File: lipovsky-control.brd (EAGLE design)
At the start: 59 x 32 mm, 44 parts, among them J5 AVRISP0.1", P1 M04-929P, P2 M04-929P, P3 M04-929P, P4 M04-929P, U1 ATTINYX4A8MU, U2 MIC2288YD5, U3 MIC2288YD5, U4 LTV-816S

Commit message: tidy
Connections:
- removed net !OE: J5.3, P3.3, U1.1
- removed net CP: J5.1, P3.2, U1.20
- removed net DS: J5.4, P3.1, U1.16
- new net !S_RESET: P3.1
- new net MISO: J5.1, U1.20
- new net SCL: J5.3, P3.2, U1.1
- new net SDA: J5.4, P3.3, U1.16
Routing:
- net !OE: track 40.7 -> 0.00 mm
- net CP: track 39.9 -> 0.00 mm
- net SDA: track 0.00 -> 38.6 mm, vias 0 -> 1
- net SCL: track 0.00 -> 38.1 mm
- net DS: track 31.9 -> 0.00 mm, vias 1 -> 0
- net MISO: track 0.00 -> 6.01 mm
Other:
- board text added: "SCL"
- board text added: "SDA"
- board text removed: "!OE"
- board text removed: "CP"
- board text removed: "DS"
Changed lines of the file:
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@@
 <wire x1="1.5" y1="8.75" x2="1.5" y2="8.25" width="0.15" layer="21"/>
 <text x="51.9" y="28.4" size="0.8" layer="21" font="vector" ratio="15" align="top-center">S-</text>
-<text x="49.3" y="28.4" size="0.8" layer="21" font="vector" ratio="15" align="top-center">!OE</text>
-<text x="46.8" y="28.4" size="0.8" layer="21" font="vector" ratio="15" align="top-center">CP</text>
-<text x="44.3" y="28.4" size="0.8" layer="21" font="vector" ratio="15" align="top-center">DS</text>
+<text x="49.3" y="28.4" size="0.8" layer="21" font="vector" ratio="15" align="top-center">SDA</text>
+<text x="46.8" y="28.4" size="0.8" layer="21" font="vector" ratio="15" align="top-center">SCL</text>
 <text x="16.2" y="28.7" size="0.8" layer="21" font="vector" ratio="15" align="top-center">+8V</text>
 <text x="18.8" y="28.7" size="0.8" layer="21" font="vector" ratio="15" align="top-center">+5V</text>
@@
 <wire x1="35.4" y1="10.84" x2="34.54" y2="11.7" width="0.3" layer="1"/>
 <wire x1="36.5" y1="2.7" x2="35.4" y2="3.8" width="0.3" layer="1"/>
-<wire x1="51.81" y1="30" x2="50.51" y2="28.7" width="0.3" layer="1"/>
-<wire x1="50.51" y1="28.7" x2="42.4" y2="28.7" width="0.3" layer="1"/>
-<wire x1="42.4" y1="28.7" x2="36.6" y2="22.9" width="0.3" layer="1"/>
-<wire x1="36.6" y1="22.9" x2="30.2" y2="22.9" width="0.3" layer="1"/>
-<wire x1="30.2" y1="22.9" x2="29.4" y2="22.1" width="0.3" layer="1"/>
-<wire x1="29.4" y1="22.1" x2="25.7" y2="22.1" width="0.3" layer="1"/>
+<wire x1="51.81" y1="30" x2="50.41" y2="28.6" width="0.3" layer="1"/>
+<wire x1="50.41" y1="28.6" x2="42.3" y2="28.6" width="0.3" layer="1"/>
+<wire x1="42.3" y1="28.6" x2="36.6" y2="22.9" width="0.3" layer="1"/>
+<wire x1="36.6" y1="22.9" x2="30.7" y2="22.9" width="0.3" layer="1"/>
+<wire x1="30.7" y1="22.9" x2="29.9" y2="22.1" width="0.3" layer="1"/>
+<wire x1="29.9" y1="22.1" x2="25.7" y2="22.1" width="0.3" layer="1"/>
 <wire x1="25.7" y1="22.1" x2="25.45" y2="22.35" width="0.3" layer="1"/>
 <wire x1="25.45" y1="22.35" x2="25.45" y2="22.55" width="0.3" layer="1"/>
@@
 <via x="20" y="28.9" extent="1-16" drill="0.35"/>
 </signal>
-<signal name="!OE">
-<contactref element="U1" pad="1"/>
-<contactref element="J5" pad="3"/>
-<contactref element="P3" pad="3"/>
-<wire x1="21.9" y1="22" x2="22.075" y2="22" width="0.25" layer="1"/>
-<wire x1="22.075" y1="22" x2="22.075" y2="20.025" width="0.25" layer="1"/>
-<wire x1="22.075" y1="20.025" x2="23.275" y2="18.825" width="0.25" layer="1"/>
-<wire x1="23.275" y1="18.825" x2="23.275" y2="17.005" width="0.25" layer="1"/>
-<wire x1="23.275" y1="17.005" x2="22" y2="15.73" width="0.25" layer="1"/>
-<wire x1="47.37" y1="28.1" x2="42.7" y2="28.1" width="0.3" layer="16"/>
-<wire x1="42.7" y1="28.1" x2="36.9" y2="22.3" width="0.3" layer="16"/>
-<wire x1="36.9" y1="22.3" x2="30.4" y2="22.3" width="0.3" layer="16"/>
-<wire x1="30.4" y1="22.3" x2="25.1" y2="17" width="0.3" layer="16"/>
-<wire x1="25.1" y1="17" x2="23.43" y2="17" width="0.3" layer="16"/>
-<wire x1="23.43" y1="17" x2="22.16" y2="15.73" width="0.3" layer="16"/>
-<wire x1="22.16" y1="15.73" x2="22" y2="15.73" width="0.3" layer="16"/>
-<wire x1="47.37" y1="28.1" x2="49.27" y2="30" width="0.3" layer="16"/>
-</signal>
-<signal name="CP">
+<signal name="MISO">
 <contactref element="U1" pad="20"/>
 <contactref element="J5" pad="1"/>
-<contactref element="P3" pad="2"/>
 <wire x1="21" y1="21.1" x2="21" y2="19.2" width="0.25" layer="1"/>
 <wire x1="21" y1="19.2" x2="20.725" y2="18.925" width="0.25" layer="1"/>
 <wire x1="20.725" y1="18.925" x2="20.725" y2="16.995" width="0.25" layer="1"/>
 <wire x1="20.725" y1="16.995" x2="19.46" y2="15.73" width="0.25" layer="1"/>
-<wire x1="45.43" y1="28.7" x2="42.4" y2="28.7" width="0.3" layer="16"/>
-<wire x1="42.4" y1="28.7" x2="36.6" y2="22.9" width="0.3" layer="16"/>
-<wire x1="36.6" y1="22.9" x2="30.2" y2="22.9" width="0.3" layer="16"/>
-<wire x1="30.2" y1="22.9" x2="26.9" y2="19.6" width="0.3" layer="16"/>
-<wire x1="26.9" y1="19.6" x2="24" y2="19.6" width="0.3" layer="16"/>
-<wire x1="24" y1="19.6" x2="23.275" y2="18.875" width="0.3" layer="16"/>
-<wire x1="23.275" y1="18.875" x2="23.275" y2="17.675" width="0.3" layer="16"/>
-<wire x1="23.275" y1="17.675" x2="22.6" y2="17" width="0.3" layer="16"/>
-<wire x1="22.6" y1="17" x2="20.73" y2="17" width="0.3" layer="16"/>
-<wire x1="20.73" y1="17" x2="19.46" y2="15.73" width="0.3" layer="16"/>
-<wire x1="45.43" y1="28.7" x2="46.73" y2="30" width="0.3" layer="16"/>
-</signal>
-<signal name="DS">
-<contactref element="U1" pad="16"/>
-<contactref element="J5" pad="4"/>
-<contactref element="P3" pad="1"/>
-<via x="20.2" y="19.6" extent="1-16" drill="0.35"/>
-<wire x1="19" y1="21.1" x2="19" y2="20.6" width="0.25" layer="1"/>
-<wire x1="19" y1="20.6" x2="19.2" y2="20.4" width="0.25" layer="1"/>
-<wire x1="19.2" y1="20.4" x2="19.9" y2="20.4" width="0.25" layer="1"/>
-<wire x1="19.9" y1="20.4" x2="20.2" y2="20.1" width="0.25" layer="1"/>
-<wire x1="20.2" y1="20.1" x2="20.2" y2="19.6" width="0.25" layer="1"/>
-<wire x1="20.67" y1="19.6" x2="22" y2="18.27" width="0.3" layer="16"/>
-<wire x1="26.7" y1="20.2" x2="30" y2="23.5" width="0.3" layer="16"/>
-<wire x1="30" y1="23.5" x2="36.3" y2="23.5" width="0.3" layer="16"/>
-<wire x1="36.3" y1="23.5" x2="42.1" y2="29.3" width="0.3" layer="16"/>
-<wire x1="26.7" y1="20.2" x2="23.83" y2="20.2" width="0.3" layer="16"/>
-<wire x1="20.67" y1="19.6" x2="20.2" y2="19.6" width="0.3" layer="16"/>
-<wire x1="23.83" y1="20.2" x2="22" y2="18.37" width="0.3" layer="16"/>
-<wire x1="22" y1="18.37" x2="22" y2="18.27" width="0.3" layer="16"/>
-<wire x1="42.1" y1="29.3" x2="43.49" y2="29.3" width="0.3" layer="16"/>
-<wire x1="43.49" y1="29.3" x2="44.19" y2="30" width="0.3" layer="16"/>
 </signal>
 <signal name="S+">
@@
 <contactref element="P1" pad="1"/>
 </signal>
+<signal name="SDA">
+<contactref element="P3" pad="3"/>
+<contactref element="U1" pad="16"/>
+<contactref element="J5" pad="4"/>
+<via x="20.2" y="19.6" extent="1-16" drill="0.35"/>
+<wire x1="19" y1="21.1" x2="19" y2="20.6" width="0.25" layer="1"/>
+<wire x1="19" y1="20.6" x2="19.2" y2="20.4" width="0.25" layer="1"/>
+<wire x1="19.2" y1="20.4" x2="19.9" y2="20.4" width="0.25" layer="1"/>
+<wire x1="19.9" y1="20.4" x2="20.2" y2="20.1" width="0.25" layer="1"/>
+<wire x1="20.2" y1="20.1" x2="20.2" y2="19.6" width="0.25" layer="1"/>
+<wire x1="20.67" y1="19.6" x2="22" y2="18.27" width="0.3" layer="16"/>
+<wire x1="27" y1="19.6" x2="30.6" y2="23.2" width="0.3" layer="16"/>
+<wire x1="30.6" y1="23.2" x2="36.5" y2="23.2" width="0.3" layer="16"/>
+<wire x1="36.5" y1="23.2" x2="42.8" y2="29.5" width="0.3" layer="16"/>
+<wire x1="42.8" y1="29.5" x2="42.8" y2="30.6" width="0.3" layer="16"/>
+<wire x1="42.8" y1="30.6" x2="43.5" y2="31.3" width="0.3" layer="16"/>
+<wire x1="27" y1="19.6" x2="23.33" y2="19.6" width="0.3" layer="16"/>
+<wire x1="20.67" y1="19.6" x2="20.2" y2="19.6" width="0.3" layer="16"/>
+<wire x1="23.33" y1="19.6" x2="22" y2="18.27" width="0.3" layer="16"/>
+<wire x1="43.5" y1="31.3" x2="47.97" y2="31.3" width="0.3" layer="16"/>
+<wire x1="47.97" y1="31.3" x2="49.27" y2="30" width="0.3" layer="16"/>
+</signal>
+<signal name="SCL">
+<contactref element="P3" pad="2"/>
+<contactref element="U1" pad="1"/>
+<contactref element="J5" pad="3"/>
+<wire x1="21.9" y1="22" x2="22.075" y2="22" width="0.25" layer="1"/>
+<wire x1="22.075" y1="22" x2="22.075" y2="20.025" width="0.25" layer="1"/>
+<wire x1="22.075" y1="20.025" x2="23.275" y2="18.825" width="0.25" layer="1"/>
+<wire x1="23.275" y1="18.825" x2="23.275" y2="17.005" width="0.25" layer="1"/>
+<wire x1="23.275" y1="17.005" x2="22" y2="15.73" width="0.25" layer="1"/>
+<wire x1="45.33" y1="28.6" x2="42.7" y2="28.6" width="0.3" layer="16"/>
+<wire x1="42.7" y1="28.6" x2="36.7" y2="22.6" width="0.3" layer="16"/>
+<wire x1="36.7" y1="22.6" x2="30.8" y2="22.6" width="0.3" layer="16"/>
+<wire x1="30.8" y1="22.6" x2="25.2" y2="17" width="0.3" layer="16"/>
+<wire x1="25.2" y1="17" x2="23.27" y2="17" width="0.3" layer="16"/>
+<wire x1="45.33" y1="28.6" x2="46.73" y2="30" width="0.3" layer="16"/>
+<wire x1="23.27" y1="17" x2="22" y2="15.73" width="0.3" layer="16"/>
+</signal>
+<signal name="!S_RESET">
+<contactref element="P3" pad="1"/>
+</signal>
 </signals>

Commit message: neverending gilding
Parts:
- added R16, R17: RES4.7K_16, dubec:0402
- moved R15 6.89 mm to (17.1, 20.2), turned to 0 degrees
- moved R3 0.20 mm to (29.6, 20.0)
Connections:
- net !RESET: now also R15.1; no longer R15.2
- net +5V: now also R15.2, R16.2, R17.1; no longer R15.1
- net SCL: now also R17.2
- net SDA: now also R16.1
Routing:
- net !RESET: track 23.3 -> 18.0 mm, vias 3 -> 2
- net SCL: track 38.1 -> 39.3 mm, vias 0 -> 1
- net +5V: track 51.0 -> 50.0 mm
- net S-: track 130.1 -> 130.7 mm
- net SDA: track 38.6 -> 39.0 mm, vias 1 -> 2

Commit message: tweaks
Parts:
- added U$2: JUMPER-PAD, dubec:JUMPER-PAD-ROUND
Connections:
- net !S_RESET: now also U$2.1
- net MISO: now also U$2.2
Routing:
- net !S_RESET: track 0.00 -> 29.0 mm, vias 0 -> 1
- net MISO: track 6.01 -> 24.5 mm
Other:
- board text added: "Enable slave reset"
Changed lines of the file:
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@@
 <text x="19.5" y="9.5" size="1" layer="21" font="vector" ratio="15" rot="SR90" align="center-left">OVER
 TEMP</text>
-<text x="1" y="11" size="1" layer="21" font="vector" ratio="15" rot="SR90" align="top-center">C1</text>
-<text x="1" y="13.5" size="1" layer="21" font="vector" ratio="15" rot="SR90" align="top-center">C2</text>
-<text x="1" y="16" size="1" layer="21" font="vector" ratio="15" rot="SR90" align="top-center">C3</text>
-<text x="1" y="18.5" size="1" layer="21" font="vector" ratio="15" rot="SR90" align="top-center">C4</text>
-<text x="1" y="21" size="1" layer="21" font="vector" ratio="15" rot="SR90" align="top-center">C5</text>
-<text x="1" y="23.5" size="1" layer="21" font="vector" ratio="15" rot="SR90" align="top-center">C6</text>
+<text x="1" y="11.1" size="1" layer="21" font="vector" ratio="15" rot="SR90" align="top-center">C1</text>
+<text x="1" y="13.6" size="1" layer="21" font="vector" ratio="15" rot="SR90" align="top-center">C2</text>
+<text x="1" y="16.1" size="1" layer="21" font="vector" ratio="15" rot="SR90" align="top-center">C3</text>
+<text x="1" y="18.6" size="1" layer="21" font="vector" ratio="15" rot="SR90" align="top-center">C4</text>
+<text x="1" y="21.1" size="1" layer="21" font="vector" ratio="15" rot="SR90" align="top-center">C5</text>
+<text x="1" y="23.6" size="1" layer="21" font="vector" ratio="15" rot="SR90" align="top-center">C6</text>
 <polygon width="0.25" layer="29">
 <vertex x="19.7" y="23.9"/>
@@
 <vertex x="18.175" y="16.3"/>
 </polygon>
+<text x="33.4" y="19.5" size="0.8" layer="22" font="vector" ratio="15" rot="MR0" align="top-center">Enable
+slave
+reset</text>
 </plain>
 <attributes>
@@
 <attribute name="DIGIKEY_PART_#" value="541-4.70KLCT-ND" x="30.9" y="22.1" size="1.778" layer="27" rot="R180" display="off"/>
 </element>
+<element name="U$2" library="dubec" package="JUMPER-PAD-ROUND" value="JUMPER-PAD" x="33.4" y="21.2" rot="MR0"/>
 </elements>
 <signals>
@@
 <wire x1="18.1" y1="16.91" x2="18.1" y2="14.6" width="0.3" layer="16"/>
 <wire x1="18.1" y1="14.6" x2="18.3" y2="14.4" width="0.3" layer="16"/>
-<wire x1="18.3" y1="14.4" x2="27.1" y2="14.4" width="0.3" layer="16"/>
-<wire x1="27.1" y1="14.4" x2="27.2" y2="14.5" width="0.3" layer="16"/>
+<wire x1="18.3" y1="14.4" x2="19.9" y2="14.4" width="0.3" layer="16"/>
+<wire x1="19.9" y1="14.4" x2="20.5" y2="13.8" width="0.3" layer="16"/>
+<wire x1="20.5" y1="13.8" x2="25.4" y2="13.8" width="0.3" layer="16"/>
+<wire x1="25.4" y1="13.8" x2="26.1" y2="14.5" width="0.3" layer="16"/>
+<wire x1="26.1" y1="14.5" x2="27.2" y2="14.5" width="0.3" layer="16"/>
 <via x="17.6" y="21.1" extent="1-16" drill="0.35"/>
 <wire x1="17.6" y1="21.1" x2="17.6" y2="28.87" width="0.3" layer="16"/>
@@
 <wire x1="20.725" y1="18.925" x2="20.725" y2="16.995" width="0.25" layer="1"/>
 <wire x1="20.725" y1="16.995" x2="19.46" y2="15.73" width="0.25" layer="1"/>
+<contactref element="U$2" pad="2"/>
+<wire x1="33.1" y1="21.2" x2="29.4" y2="21.2" width="0.3" layer="16"/>
+<wire x1="29.4" y1="21.2" x2="26.5" y2="18.3" width="0.3" layer="16"/>
+<wire x1="26.5" y1="18.3" x2="26.5" y2="15.8" width="0.3" layer="16"/>
+<wire x1="26.5" y1="15.8" x2="25.1" y2="14.4" width="0.3" layer="16"/>
+<wire x1="25.1" y1="14.4" x2="20.79" y2="14.4" width="0.3" layer="16"/>
+<wire x1="20.79" y1="14.4" x2="19.46" y2="15.73" width="0.3" layer="16"/>
 </signal>
 <signal name="S+">
@@
 <signal name="!S_RESET">
 <contactref element="P3" pad="1"/>
+<contactref element="U$2" pad="1"/>
+<via x="50.525" y="31" extent="1-16" drill="0.35"/>
+<wire x1="44.19" y1="30" x2="45.49" y2="31.3" width="0.3" layer="1"/>
+<wire x1="45.49" y1="31.3" x2="50.325" y2="31.3" width="0.3" layer="1"/>
+<wire x1="50.325" y1="31.3" x2="50.525" y2="31.1" width="0.3" layer="1"/>
+<wire x1="50.525" y1="31.1" x2="50.525" y2="31" width="0.3" layer="1"/>
+<wire x1="50.525" y1="31" x2="50.525" y2="29.2" width="0.3" layer="16"/>
+<wire x1="50.525" y1="29.2" x2="49.325" y2="28" width="0.3" layer="16"/>
+<wire x1="49.325" y1="28" x2="42.9" y2="28" width="0.3" layer="16"/>
+<wire x1="42.9" y1="28" x2="36.1" y2="21.2" width="0.3" layer="16"/>
+<wire x1="36.1" y1="21.2" x2="33.7" y2="21.2" width="0.3" layer="16"/>
 </signal>
 </signals>

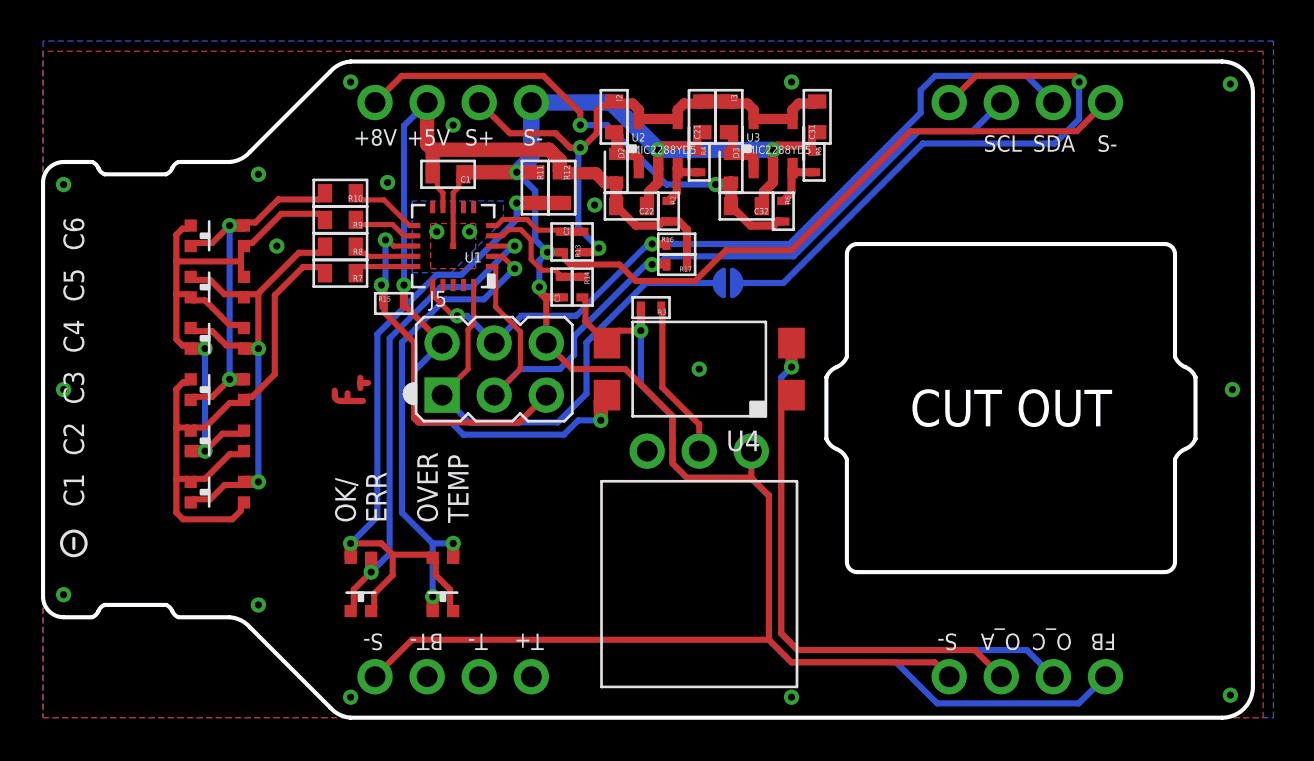
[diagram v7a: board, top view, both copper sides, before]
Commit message: Connector pin reordering
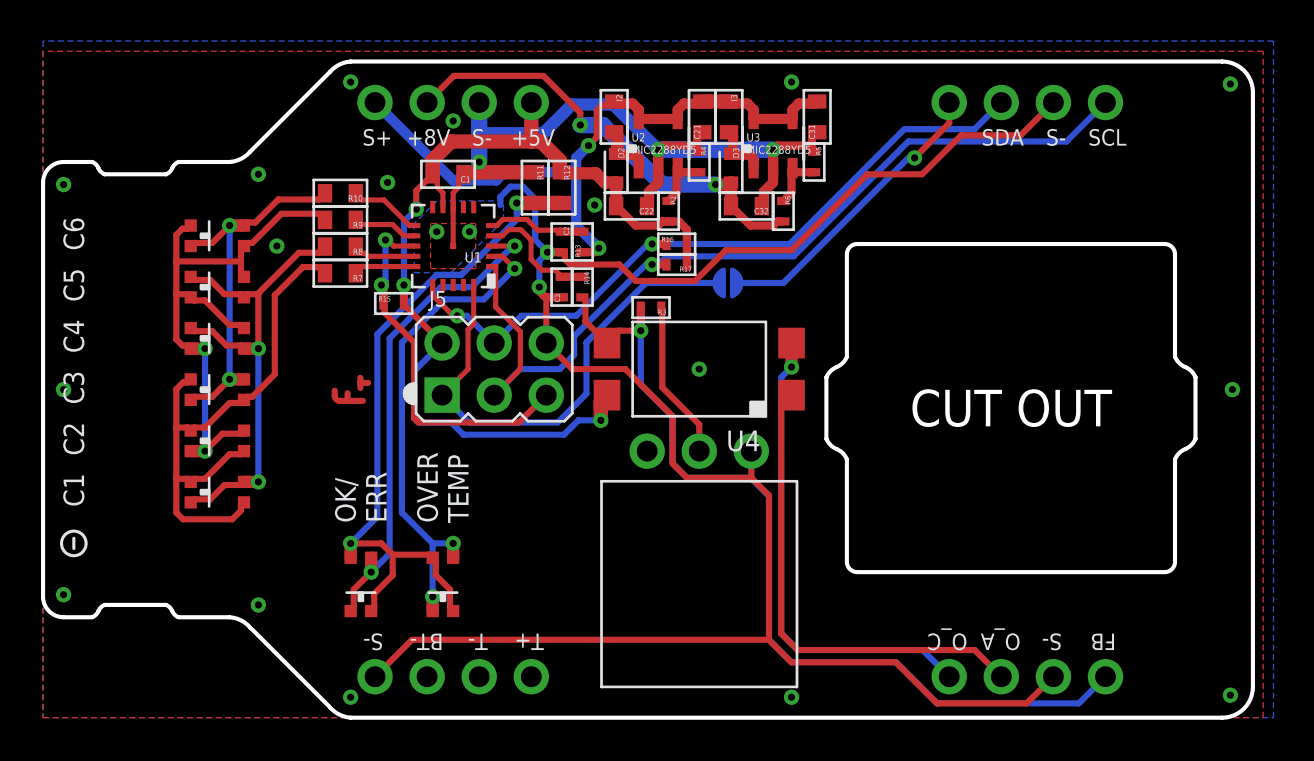
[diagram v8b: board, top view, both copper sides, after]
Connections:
- net +5V: now also P4.4; no longer P4.2
- net +8V: now also P4.2; no longer P4.1
- net OPTO_C: now also P2.4; no longer P2.2
- net S+: now also P4.1; no longer P4.3
- net S-: now also P2.2, P3.3, P4.3; no longer P2.4, P3.4, P4.4
- net SCL: now also P3.4; no longer P3.2
- net SDA: now also P3.2; no longer P3.3
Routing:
- net !S_RESET: track 29.0 -> 14.7 mm
- net S-: track 130.7 -> 138.0 mm
- net S+: track 27.7 -> 33.4 mm
- net OPTO_C: track 28.5 -> 23.4 mm
- net SCL: track 39.3 -> 44.4 mm
- net SDA: track 39.0 -> 34.8 mm
- net +5V: track 50.5 -> 46.7 mm, vias 2 -> 3
- net +8V: track 24.7 -> 22.1 mm
